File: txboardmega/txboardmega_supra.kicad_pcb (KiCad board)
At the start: 2 copper layers, 150 x 77 mm, 33 parts, among them J1 Power, J10 Switch 2, J11 Switch 3, J12 Switch 4, J13 Switch 5, J14 Switch 6, J15 Encoder, J16 TX Module, J17 Trim 1, J18 Trim 2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

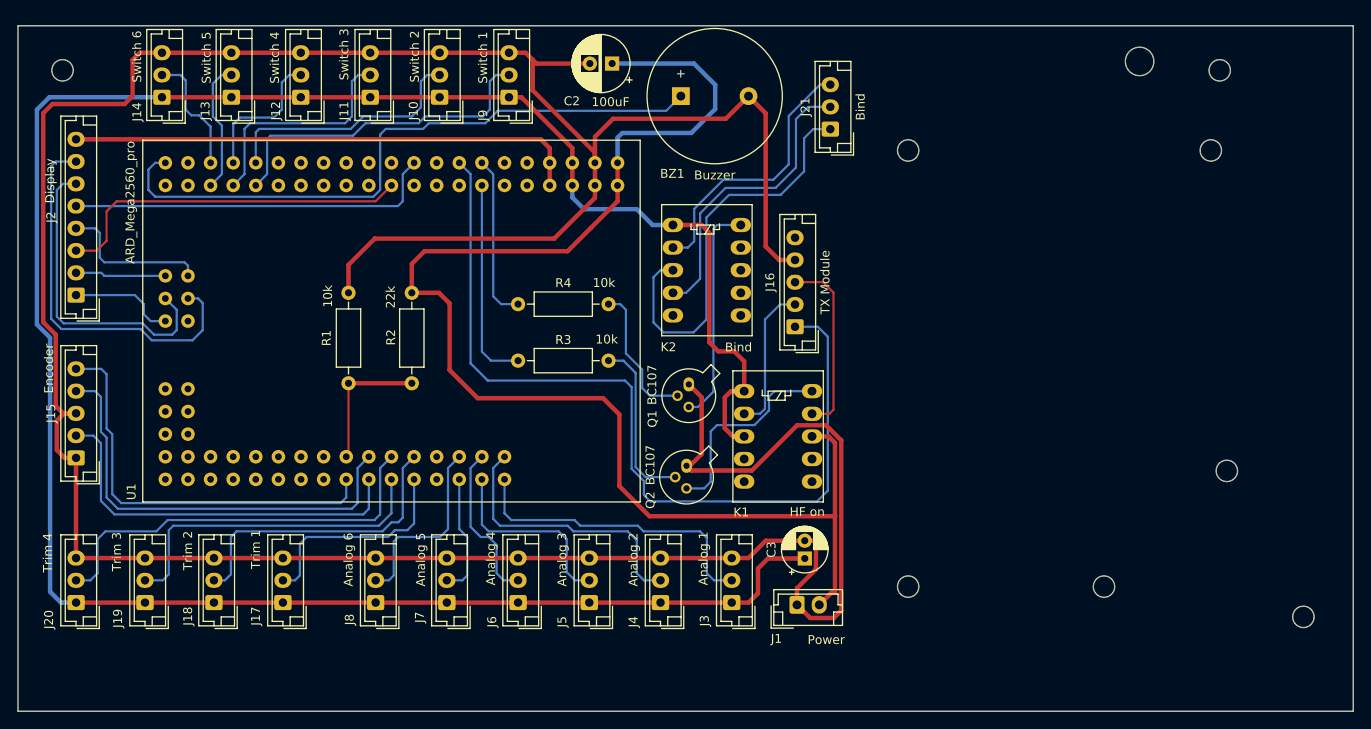
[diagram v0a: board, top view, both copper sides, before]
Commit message: Added Ports and Buzzer
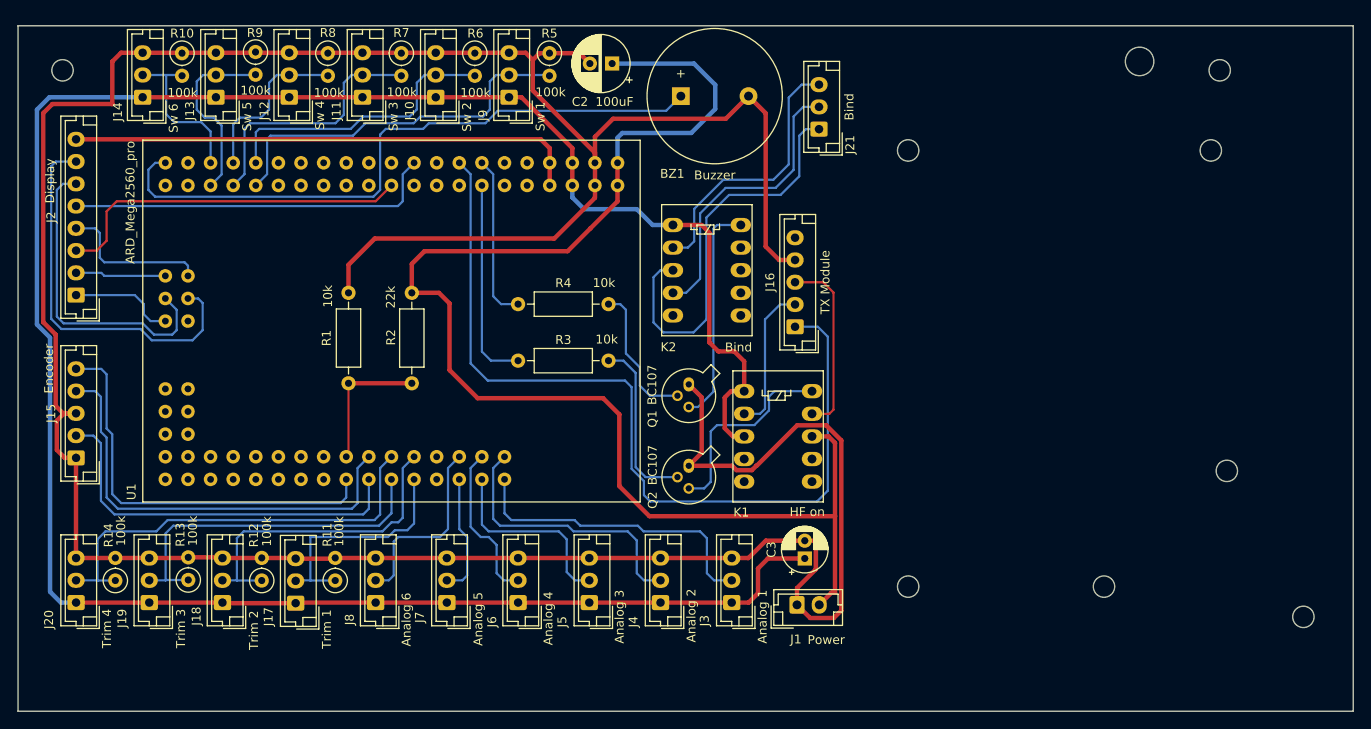
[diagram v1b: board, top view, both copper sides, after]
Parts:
- added R10: 100k, Resistor_THT:R_Axial_DIN0207_L6.3mm_D2.5mm_P2.54mm_Vertical, F.Cu at (98.4, 76.1)
- added R11: 100k, Resistor_THT:R_Axial_DIN0207_L6.3mm_D2.5mm_P2.54mm_Vertical, F.Cu at (115.6, 135.3)
- added R12: 100k, Resistor_THT:R_Axial_DIN0207_L6.3mm_D2.5mm_P2.54mm_Vertical, F.Cu at (107.4, 135.3)
- added R13: 100k, Resistor_THT:R_Axial_DIN0207_L6.3mm_D2.5mm_P2.54mm_Vertical, F.Cu at (99.1, 135.3)
- added R14: 100k, Resistor_THT:R_Axial_DIN0207_L6.3mm_D2.5mm_P2.54mm_Vertical, F.Cu at (90.9, 135.3)
- added R5: 100k, Resistor_THT:R_Axial_DIN0207_L6.3mm_D2.5mm_P2.54mm_Vertical, F.Cu at (139.7, 76.1)
- added R6: 100k, Resistor_THT:R_Axial_DIN0207_L6.3mm_D2.5mm_P2.54mm_Vertical, F.Cu at (131.3, 76.1)
- added R7: 100k, Resistor_THT:R_Axial_DIN0207_L6.3mm_D2.5mm_P2.54mm_Vertical, F.Cu at (123.1, 76.1)
- added R8: 100k, Resistor_THT:R_Axial_DIN0207_L6.3mm_D2.5mm_P2.54mm_Vertical, F.Cu at (114.8, 76.1)
- added R9: 100k, Resistor_THT:R_Axial_DIN0207_L6.3mm_D2.5mm_P2.54mm_Vertical, F.Cu at (106.7, 75.9)
- J10: value Switch 2 -> Sw 2
- J11: value Switch 3 -> Sw 3
- J12: value Switch 4 -> Sw 4
- J13: value Switch 5 -> Sw 5
- J14: value Switch 6 -> Sw 6
- J9: value Switch 1 -> Sw 1
- moved J14 2.17 mm to (94.0, 81.0)
- moved J13 1.74 mm to (102.2, 81.0)
- moved J17 1.43 mm to (111.2, 137.9)
- moved J12 1.30 mm to (110.5, 81.0)
- moved J21 1.27 mm to (170.0, 84.6)
- moved J18 0.95 mm to (103.0, 137.8)
- moved J11 0.87 mm to (118.7, 81.0)
- moved J19 0.48 mm to (94.7, 137.8)
- moved J10 0.43 mm to (126.9, 81.0)
- moved Q2 0.25 mm to (155.4, 122.4)
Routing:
- net Net-(J13-Pad2): track 14.9 -> 20.9 mm
- net Net-(J11-Pad2): track 25.8 -> 30.5 mm
- net Net-(J9-Pad2): track 37.8 -> 42.3 mm
- net Net-(J10-Pad2): track 28.5 -> 32.9 mm
- net Net-(J14-Pad2): track 13.9 -> 18.2 mm
- net Net-(J12-Pad2): track 16.0 -> 19.0 mm
- net Net-(J20-Pad2): track 46.5 -> 48.9 mm
- net Net-(J19-Pad2): track 37.5 -> 39.8 mm
- net Net-(J17-Pad2): track 24.4 -> 26.6 mm
- net Net-(J18-Pad2): track 34.0 -> 36.1 mm
- net Net-(J21-Pad2): track 33.8 -> 32.9 mm
- net Net-(J21-Pad1): track 46.3 -> 45.5 mm
- net Net-(BZ1-Pad2): track 366.9 -> 367.5 mm
